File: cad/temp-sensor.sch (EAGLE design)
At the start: 2 parts, among them U1 SE555D, U2 SE555D

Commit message: Add files via upload
test
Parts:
- added R1: (no value), rcl:R-EU_0204/7
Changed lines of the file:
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@@
 <part name="P+2" library="supply1" library_urn="urn:adsk.eagle:library:371" deviceset="VCC" device=""/>
 <part name="P+1" library="supply1" library_urn="urn:adsk.eagle:library:371" deviceset="+5V" device=""/>
+<part name="R1" library="rcl" library_urn="urn:adsk.eagle:library:334" deviceset="R-EU_" device="0204/7" package3d_urn="urn:adsk.eagle:package:23498/2"/>
 </parts>
 <sheets>
@@
 <instance part="P+1" gate="1" x="60.96" y="50.8" smashed="yes">
 <attribute name="VALUE" x="63.5" y="53.34" size="1.778" layer="96" rot="R180"/>
+</instance>
+<instance part="R1" gate="G$1" x="38.1" y="7.62" smashed="yes">
+<attribute name="NAME" x="34.29" y="9.1186" size="1.778" layer="95"/>
+<attribute name="VALUE" x="34.29" y="4.318" size="1.778" layer="96"/>
 </instance>
 </instances>
@@
 will not be understood (or retained) with this version.
 </note>
+<note version="8.3" severity="warning">
+Since Version 8.3, EAGLE supports the association of 3D packages
+with devices in libraries, schematics, and board files. Those 3D
+packages will not be understood (or retained) with this version.
+</note>
+<note version="8.4" severity="warning">
+Since Version 8.4, EAGLE supports properties for SPICE simulation.
+Probes in schematics and SPICE mapping objects found in parts and library devices
+will not be understood with this version. Update EAGLE to the latest version
+for full support of SPICE simulation.
+</note>
 </compatibility>

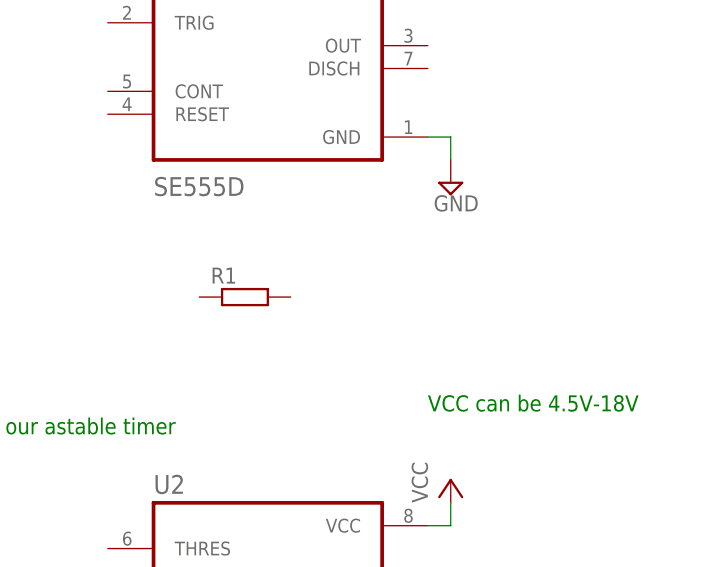
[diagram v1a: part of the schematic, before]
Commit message: stuff
add resistor
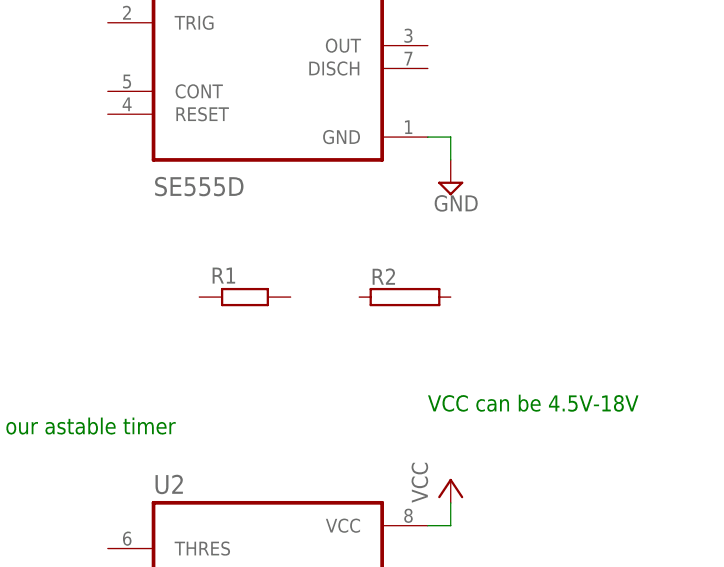
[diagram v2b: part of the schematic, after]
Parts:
- added R2: (no value), resistor-power:RAC01
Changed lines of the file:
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@@
 <part name="P+1" library="supply1" library_urn="urn:adsk.eagle:library:371" deviceset="+5V" device=""/>
 <part name="R1" library="rcl" library_urn="urn:adsk.eagle:library:334" deviceset="R-EU_" device="0204/7" package3d_urn="urn:adsk.eagle:package:23498/2"/>
+<part name="R2" library="resistor-power" library_urn="urn:adsk.eagle:library:344" deviceset="R" device="AC01" package3d_urn="urn:adsk.eagle:package:25124/1"/>
 </parts>
 <sheets>
@@
 <attribute name="VALUE" x="34.29" y="4.318" size="1.778" layer="96"/>
 </instance>
+<instance part="R2" gate="G$1" x="55.88" y="7.62" smashed="yes">
+<attribute name="NAME" x="52.07" y="8.9916" size="1.778" layer="95"/>
+<attribute name="VALUE" x="52.07" y="4.699" size="1.778" layer="96"/>
+</instance>
 </instances>

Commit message: Test
Test1 delete resistor
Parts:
- removed R1: (no value), rcl:R-EU_0204/7
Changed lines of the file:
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@@
 <part name="P+2" library="supply1" library_urn="urn:adsk.eagle:library:371" deviceset="VCC" device=""/>
 <part name="P+1" library="supply1" library_urn="urn:adsk.eagle:library:371" deviceset="+5V" device=""/>
-<part name="R1" library="rcl" library_urn="urn:adsk.eagle:library:334" deviceset="R-EU_" device="0204/7" package3d_urn="urn:adsk.eagle:package:23498/2"/>
 <part name="R2" library="resistor-power" library_urn="urn:adsk.eagle:library:344" deviceset="R" device="AC01" package3d_urn="urn:adsk.eagle:package:25124/1"/>
 </parts>
@@
 <instance part="P+1" gate="1" x="60.96" y="50.8" smashed="yes">
 <attribute name="VALUE" x="63.5" y="53.34" size="1.778" layer="96" rot="R180"/>
-</instance>
-<instance part="R1" gate="G$1" x="38.1" y="7.62" smashed="yes">
-<attribute name="NAME" x="34.29" y="9.1186" size="1.778" layer="95"/>
-<attribute name="VALUE" x="34.29" y="4.318" size="1.778" layer="96"/>
 </instance>
 <instance part="R2" gate="G$1" x="55.88" y="7.62" smashed="yes">
@@
 packages will not be understood (or retained) with this version.
 </note>
-<note version="8.4" severity="warning">
-Since Version 8.4, EAGLE supports properties for SPICE simulation.
-Probes in schematics and SPICE mapping objects found in parts and library devices
-will not be understood with this version. Update EAGLE to the latest version
-for full support of SPICE simulation.
-</note>
 </compatibility>

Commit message: initialized schematic
LTSpice implementation
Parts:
- removed R2: (no value), resistor-power:RAC01
- added C1: 1u, 1uF cap:CL10B105KP8NNNC
- added C2, C3: 10nF, 10nF Cap:GRM155R71E103KA01D
- added IC1, IC2, IC3: 320S14-U, 320S14-U:320S14-U
- added OPAMP1, OPAMP2, OPAMP3, OPAMP4: MCP6001UT-I/OT, MCP600:MCP6001UT-I/OT
- added Q1: 300S14-U, 300S14-U:300S14-U
- added R1, R3, R8, R9: 1k, 95ohm:ERJ-2RKF95R3X
- added R4, R5: 5k, 95ohm:ERJ-2RKF95R3X
- added R6: 40k, 95ohm:ERJ-2RKF95R3X
- added R7: 10k, 10kohm:RC0603FR-0710KL
- added RPTAT1: 1.76k, 1.76k ohm:RT0603BRD071K76L
- added RVBE1: 95.3, 95ohm:ERJ-2RKF95R3X
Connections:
- new net N$1: IC2.E2, R3.1
- new net N$10: IC1.C1, IC2.C2, OPAMP3.VIN+, R4.2
- new net N$11: IC1.C2, OPAMP4.VIN+, R5.2
- new net N$12: IC3.B2, IC3.C1, R6.2
- new net N$13: OPAMP3.VIN-, OPAMP3.VOUT, R7.2, R8.2
- new net N$14: OPAMP4.VIN-, OPAMP4.VOUT, U1.CONT
- new net N$15: C1.2, R7.1, U1.DISCH, U1.THRES
- new net N$16: R8.1, R9.2, U2.DISCH
- new net N$17: C2.2, R9.1, U2.THRES, U2.TRIG
- new net N$18: C3.2, U2.CONT
- new net N$19: U1.OUT
- new net N$2: IC2.E1, R1.1
- new net N$20: U2.OUT
- new net N$3: IC2.B1, IC2.B2, OPAMP2.VOUT
- new net N$4: IC2.C1, OPAMP2.VIN+, RPTAT1.2
- new net N$5: IC1.E1, IC1.E2, IC1.E3, IC1.E4, IC3.E1, IC3.E2, R1.2, R3.2
- new net N$6: IC1.B1, IC1.B2, IC1.B3, IC1.B4, IC3.B1, OPAMP1.VOUT
- new net N$7: IC1.C4, OPAMP1.VIN+, RVBE1.2
- new net N$8: IC1.C3, IC3.C2, OPAMP1.VIN-, OPAMP2.VIN-, Q1.B1, Q1.C1
- new net N$9: Q1.B2, Q1.B3, Q1.B4, Q1.C2, Q1.C3, Q1.C4, RVBE1.1
- net GND: now also C1.1, C2.1, C3.1, Q1.E1, Q1.E2, Q1.E3, Q1.E4, R4.1, R5.1, R6.1, RPTAT1.1
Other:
- moved on the sheet: U1, U2

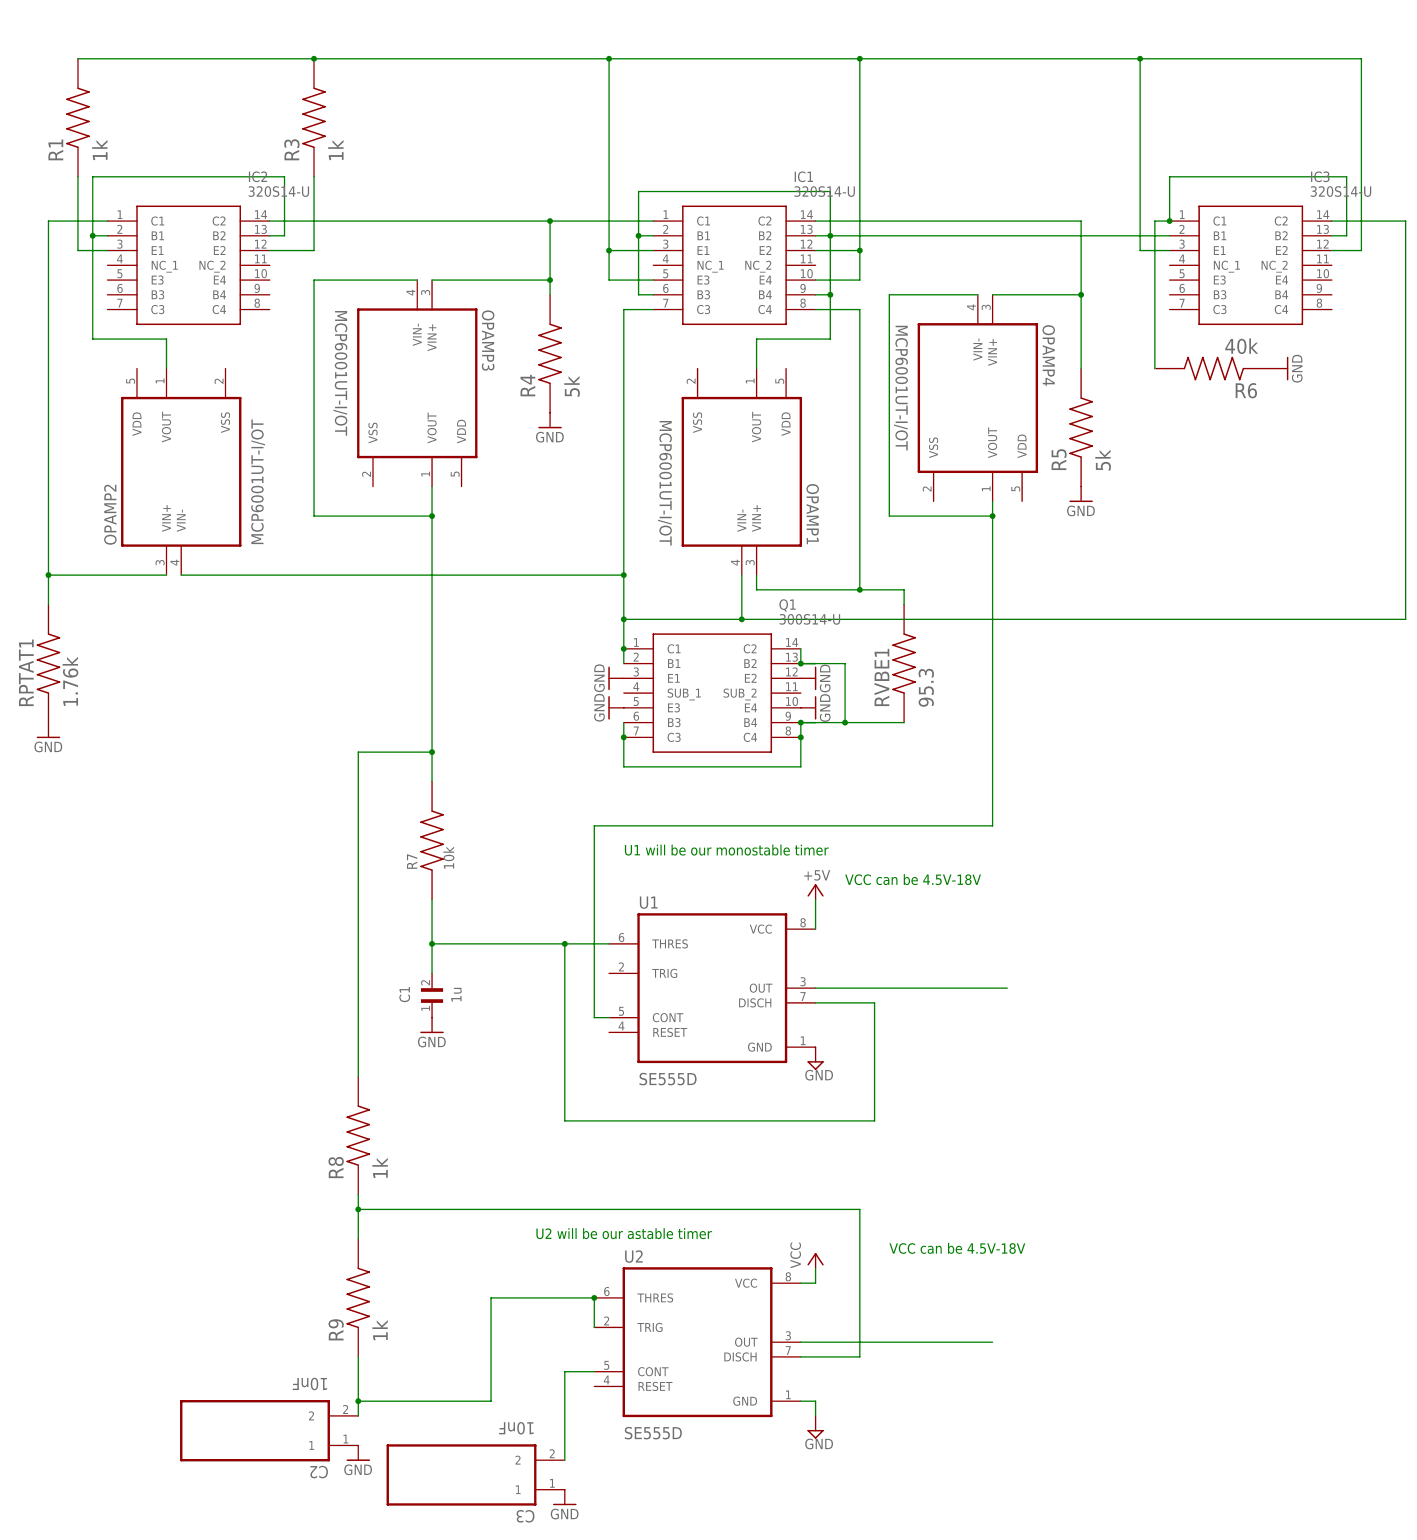
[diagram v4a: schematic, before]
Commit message: Spencer's schematic additions
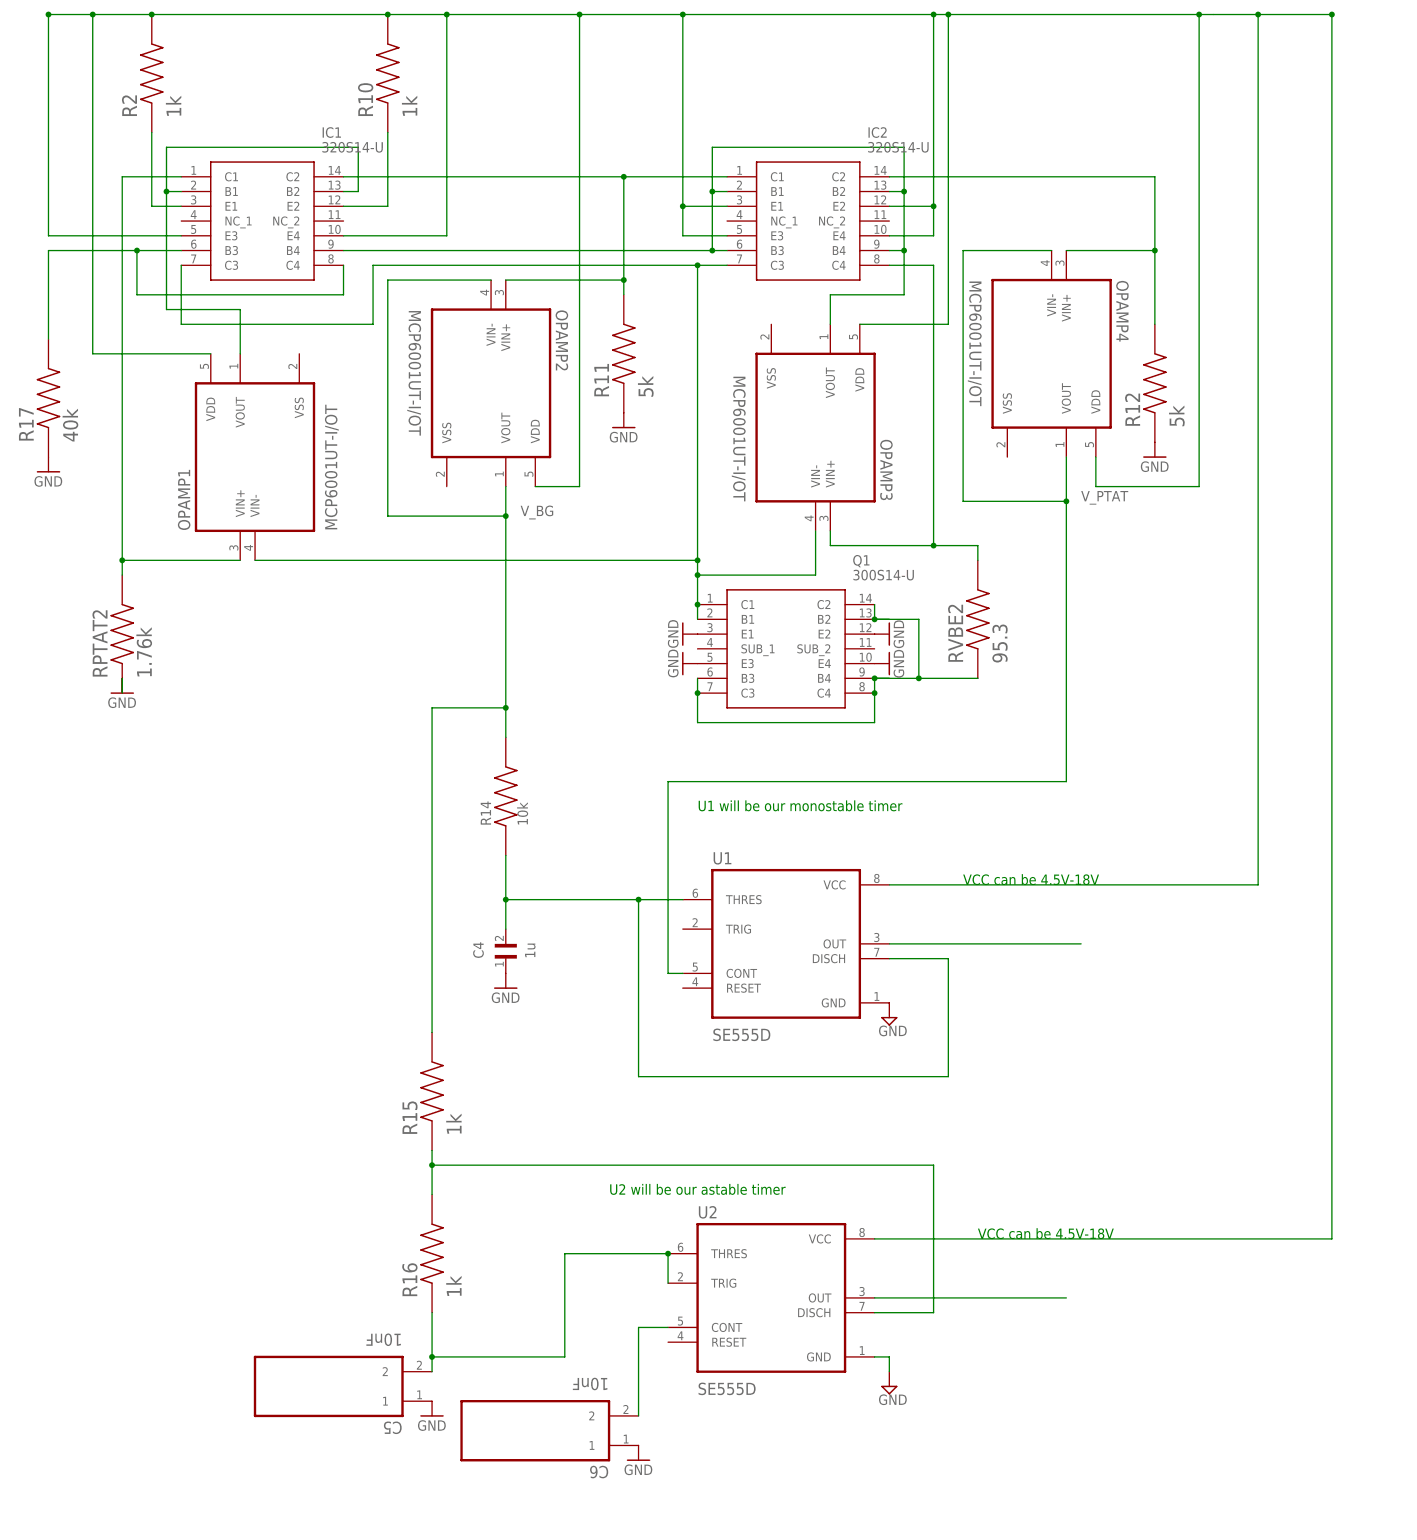
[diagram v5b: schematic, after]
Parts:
- removed C1: 1u, 1uF cap:CL10B105KP8NNNC
- removed C2, C3: 10nF, 10nF Cap:GRM155R71E103KA01D
- removed IC3: 320S14-U, 320S14-U:320S14-U
- removed R1, R3, R8, R9: 1k, 95ohm:ERJ-2RKF95R3X
- removed R4, R5: 5k, 95ohm:ERJ-2RKF95R3X
- removed R6: 40k, 95ohm:ERJ-2RKF95R3X
- removed R7: 10k, 10kohm:RC0603FR-0710KL
- removed RPTAT1: 1.76k, 1.76k ohm:RT0603BRD071K76L
- removed RVBE1: 95.3, 95ohm:ERJ-2RKF95R3X
- added C4: 1u, 1uF cap:CL10B105KP8NNNC
- added C5, C6: 10nF, 10nF Cap:GRM155R71E103KA01D
- added R10, R15, R16, R2: 1k, 95ohm:ERJ-2RKF95R3X
- added R11, R12: 5k, 95ohm:ERJ-2RKF95R3X
- added R14: 10k, 10kohm:RC0603FR-0710KL
- added R17: 40k, 95ohm:ERJ-2RKF95R3X
- added RPTAT2: 1.76k, 1.76k ohm:RT0603BRD071K76L
- added RVBE2: 95.3, 95ohm:ERJ-2RKF95R3X
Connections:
- removed net +5V: U1.VCC
- removed net N$1: IC2.E2, R3.1
- removed net N$12: IC3.B2, IC3.C1, R6.2
- removed net N$13: OPAMP3.VIN-, OPAMP3.VOUT, R7.2, R8.2
- removed net N$15: C1.2, R7.1, U1.DISCH, U1.THRES
- removed net N$16: R8.1, R9.2, U2.DISCH
- removed net N$17: C2.2, R9.1, U2.THRES, U2.TRIG
- removed net N$18: C3.2, U2.CONT
- removed net N$2: IC2.E1, R1.1
- removed net N$3: IC2.B1, IC2.B2, OPAMP2.VOUT
- removed net N$4: IC2.C1, OPAMP2.VIN+, RPTAT1.2
- removed net N$5: IC1.E1, IC1.E2, IC1.E3, IC1.E4, IC3.E1, IC3.E2, R1.2, R3.2
- removed net N$6: IC1.B1, IC1.B2, IC1.B3, IC1.B4, IC3.B1, OPAMP1.VOUT
- removed net N$7: IC1.C4, OPAMP1.VIN+, RVBE1.2
- removed net N$8: IC1.C3, IC3.C2, OPAMP1.VIN-, OPAMP2.VIN-, Q1.B1, Q1.C1
- removed net N$9: Q1.B2, Q1.B3, Q1.B4, Q1.C2, Q1.C3, Q1.C4, RVBE1.1
- removed net VCC: U2.VCC
- new net N$21: IC1.B1, IC1.B2, OPAMP1.VOUT
- new net N$22: IC1.C1, OPAMP1.VIN+, RPTAT2.2
- new net N$23: IC1.E3, IC1.E4, IC2.E1, IC2.E2, IC2.E3, IC2.E4, OPAMP1.VDD, OPAMP2.VDD, OPAMP3.VDD, OPAMP4.VDD, R10.2, R2.2, U1.VCC, U2.VCC
- new net N$24: IC1.B4, IC2.B1, IC2.B2, IC2.B3, IC2.B4, OPAMP3.VOUT
- new net N$25: IC1.C3, IC2.C3, OPAMP1.VIN-, OPAMP3.VIN-, Q1.B1, Q1.C1
- new net N$26: Q1.B2, Q1.B3, Q1.B4, Q1.C2, Q1.C3, Q1.C4, RVBE2.1
- new net N$27: IC2.C4, OPAMP3.VIN+, RVBE2.2
- new net N$29: OPAMP2.VIN-, OPAMP2.VOUT, R14.2, R15.2
- new net N$31: C4.2, R14.1, U1.DISCH, U1.THRES
- new net N$32: R15.1, R16.2, U2.DISCH
- new net N$33: C5.2, R16.1, U2.THRES, U2.TRIG
- new net N$34: C6.2, U2.CONT
- new net N$39: IC1.B3, IC1.C4, R17.2
- new net V_BG: IC1.C2, IC2.C1, OPAMP2.VIN+, R11.2
- new net V_PTAT: IC2.C2, OPAMP4.VIN+, R12.2
- net GND: now also C4.1, C5.1, C6.1, R11.1, R12.1, R17.1, RPTAT2.1; no longer C1.1, C2.1, C3.1, R4.1, R5.1, R6.1, RPTAT1.1
- net N$10: now also IC1.E2, R10.1; no longer IC1.C1, IC2.C2, OPAMP3.VIN+, R4.2
- net N$11: now also IC1.E1, R2.1; no longer IC1.C2, OPAMP4.VIN+, R5.2
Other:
- moved on the sheet: IC1, IC2, OPAMP1, OPAMP2, OPAMP3, OPAMP4, Q1, U1, U2

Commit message: Add files via upload
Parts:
- removed R14: 10k, 10kohm:RC0603FR-0710KL
- removed R15, R16: 1k, 95ohm:ERJ-2RKF95R3X
- removed R17: 40k, 95ohm:ERJ-2RKF95R3X
- removed RPTAT2: 1.76k, 1.76k ohm:RT0603BRD071K76L
- removed RVBE2: 95.3, 95ohm:ERJ-2RKF95R3X
- added C1, C10, C2: 10nF, SparkFun-Capacitors:10NF-0603-50V-10%
- added C3, C7, C8, C9: 0.1uF, SparkFun-Capacitors:0.1UF-0603-25V-10%-X7R-WE
- added R1, R3, R8, R9: 1k, SparkFun-Resistors:1KOHM-0603-1/10W-1%
- added R4, R5, R6: 100k, SparkFun-Resistors:100KOHM-0603-1/10W-1%
- added R7: 5.1k, SparkFun-Resistors:5.1KOHM5.1KOHM-0603-1/10W-1%
- C4: value 1u -> 1.0uF; device 1uF cap:CL10B105KP8NNNC -> SparkFun-Capacitors:1.0UF-0603-16V-10%-X7R
- C5, C6: value 10nF -> 0.1uF; device 10nF Cap:GRM155R71E103KA01D -> SparkFun-Capacitors:0.1UF-0603-25V-10%-X7R-WE
- R10, R2: device 95ohm:ERJ-2RKF95R3X -> SparkFun-Resistors:1KOHM-0603-1/10W-1%
- R11: value 5k -> 5.1k; device 95ohm:ERJ-2RKF95R3X -> SparkFun-Resistors:5.1KOHM5.1KOHM-0603-1/10W-1%
- R12: value 5k -> 10k; device 95ohm:ERJ-2RKF95R3X -> SparkFun-Resistors:10KOHM-0603-1/10W-1%
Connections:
- net N$35 renamed PULSE_OUT
- net N$36 renamed FREQ_OUT
- removed net N$10: IC1.E2, R10.1
- removed net N$21: IC1.B1, IC1.B2, OPAMP1.VOUT
- removed net N$22: IC1.C1, OPAMP1.VIN+, RPTAT2.2
- removed net N$23: IC1.E3, IC1.E4, IC2.E1, IC2.E2, IC2.E3, IC2.E4, OPAMP1.VDD, OPAMP2.VDD, OPAMP3.VDD, OPAMP4.VDD, R10.2, R2.2, U1.VCC, U2.VCC
- removed net N$24: IC1.B4, IC2.B1, IC2.B2, IC2.B3, IC2.B4, OPAMP3.VOUT
- removed net N$25: IC1.C3, IC2.C3, OPAMP1.VIN-, OPAMP3.VIN-, Q1.B1, Q1.C1
- removed net N$26: Q1.B2, Q1.B3, Q1.B4, Q1.C2, Q1.C3, Q1.C4, RVBE2.1
- removed net N$27: IC2.C4, OPAMP3.VIN+, RVBE2.2
- removed net N$29: OPAMP2.VIN-, OPAMP2.VOUT, R14.2, R15.2
- removed net N$30: OPAMP4.VIN-, OPAMP4.VOUT, U1.CONT
- removed net N$31: C4.2, R14.1, U1.DISCH, U1.THRES
- removed net N$32: R15.1, R16.2, U2.DISCH
- removed net N$33: C5.2, R16.1, U2.THRES, U2.TRIG
- removed net N$34: C6.2, U2.CONT
- removed net N$39: IC1.B3, IC1.C4, R17.2
- removed net V_BG: IC1.C2, IC2.C1, OPAMP2.VIN+, R11.2
- removed net V_PTAT: IC2.C2, OPAMP4.VIN+, R12.2
- new net +5V: C3.1, C5.1, C6.1, C7.1, C8.1, C9.1, OPAMP1.VDD, OPAMP2.VDD, OPAMP3.VDD, OPAMP4.VDD, R1.2, R3.2, U1.RESET, U1.VCC, U2.RESET, U2.VCC
- new net 3_NPN_DIODE: Q1.B1, Q1.B3, Q1.B4, Q1.C1, Q1.C3, Q1.C4, R8.1
- new net BG_REF_FD_BK: OPAMP2.VIN-, R4.1, R6.2
- new net CTAT_BASE: IC1.B1, IC1.B3, OPAMP1.VOUT
- new net CTAT_E1: IC1.E1, R3.1
- new net CTAT_E3: IC1.E3, R1.1
- new net CTAT_IN+: IC1.C3, OPAMP1.VIN+, R2.2
- new net FREQ_DIS: R10.1, R9.2, U2.DISCH
- new net FREQ_THRES: C2.1, R9.1, U2.THRES, U2.TRIG
- new net I_BG: IC1.C1, IC2.C1, OPAMP2.VIN+, R7.2
- new net I_PTAT: IC2.C3, OPAMP4.VIN+, R11.2
- new net N$1: R5.2, R6.1
- new net N$12: U2.GND
- new net N$2: IC2.E3
- new net N$3: IC2.E1
- new net N$4: IC2.E4
- new net N$5: IC2.E2
- new net N$6: C1.1, U2.CONT
- new net PTAT_BASE: IC2.B1, IC2.B2, IC2.B3, IC2.B4, OPAMP3.VOUT
- new net PTAT_IN+: IC2.C2, OPAMP3.VIN+, R8.2
- new net PULSE_THRES: C4.1, R12.1, U1.DISCH, U1.THRES
- new net TEMP_VBE: IC1.C4, IC2.C4, OPAMP1.VIN-, OPAMP3.VIN-, Q1.B2, Q1.C2
- new net VBG_REF: OPAMP2.VOUT, R10.2, R12.2, R4.2
- new net VPTAT_REF: C10.1, OPAMP4.VIN-, OPAMP4.VOUT, U1.CONT
- net GND: now also C1.2, C10.2, C2.2, C3.2, C5.2, C6.2, C7.2, C8.2, C9.2, OPAMP1.VSS, OPAMP2.VSS, OPAMP3.VSS, OPAMP4.VSS, R2.1, R5.1, R7.1; no longer C4.1, C5.1, C6.1, R12.1, R17.1, RPTAT2.1, U1.GND, U2.GND
- net N$11: now also C4.2, U1.GND; no longer IC1.E1, R2.1
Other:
- note added: "CTAT circuit"
- note added: "PTAT circuit"
- note added: "Startup circuit"
- note added: "V_BG Buffer"
- note added: "V_PTAT Buffer"
- note removed: "U2 will be our astable timer"
- note removed: "VCC can be 4.5V-18V"
- moved on the sheet: C4, IC2, OPAMP1, OPAMP2, OPAMP3, OPAMP4, Q1, R10, R12, R2, U1, U2
